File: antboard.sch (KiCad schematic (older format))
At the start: 0 parts

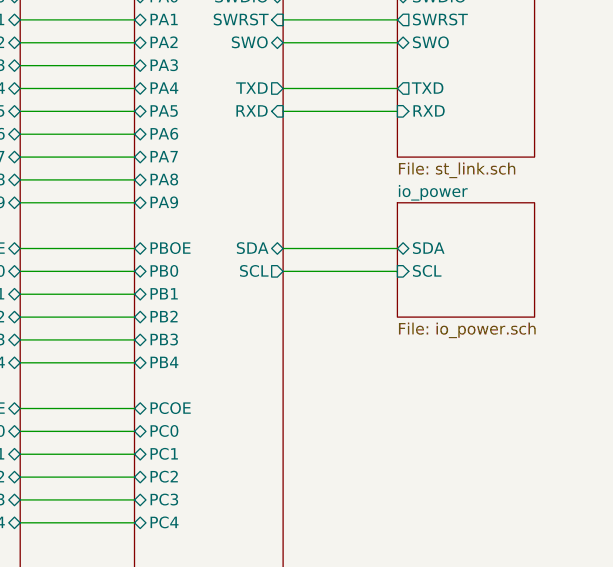
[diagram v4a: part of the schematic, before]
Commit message: sch, pcb: Add ADC to read set IO voltages
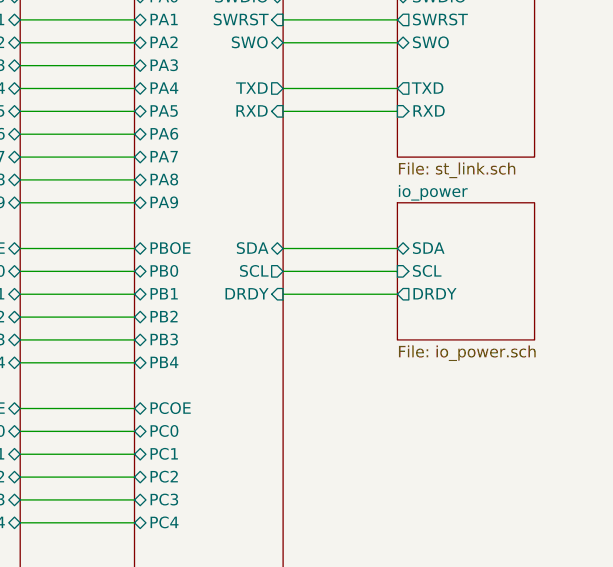
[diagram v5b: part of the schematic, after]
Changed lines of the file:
@@
 F31 "SDA" B R 5900 3600 50
 F32 "SCL" O R 5900 3700 50
+F33 "DRDY" I R 5900 3800 50
 $EndSheet
 $Sheet
@@
 $EndSheet
 $Sheet
-S 6400 3400 600  500
+S 6400 3400 600  600
 U 5EA8F1AB
 F0 "io_power" 50
@@
 F2 "SDA" B L 6400 3600 50
 F3 "SCL" I L 6400 3700 50
+F4 "DRDY" O L 6400 3800 50
 $EndSheet
 Wire Wire Line
@@
 Wire Wire Line
 	6400 3700 5900 3700
+Wire Wire Line
+	5900 3800 6400 3800
 $EndSCHEMATC

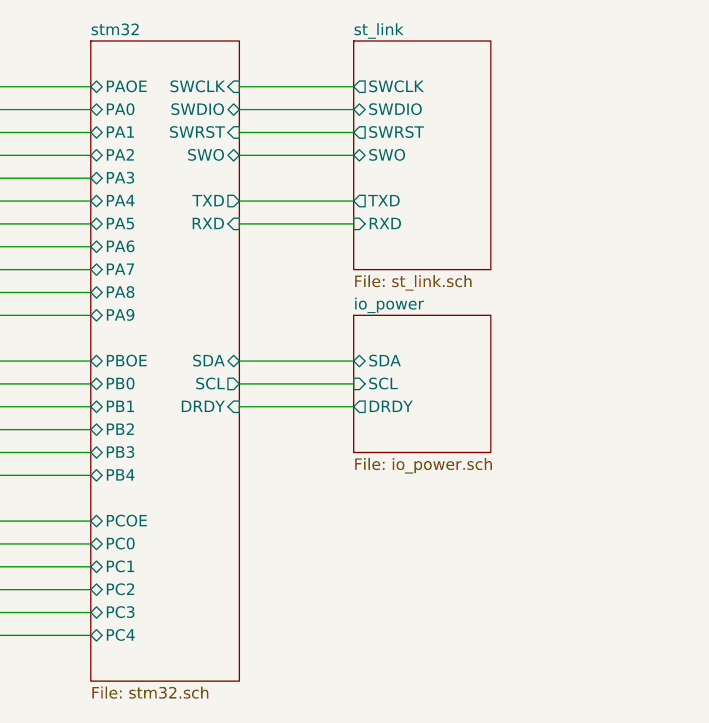
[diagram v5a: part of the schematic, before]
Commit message: sch, pcb: Add USB hub to have a single USB port
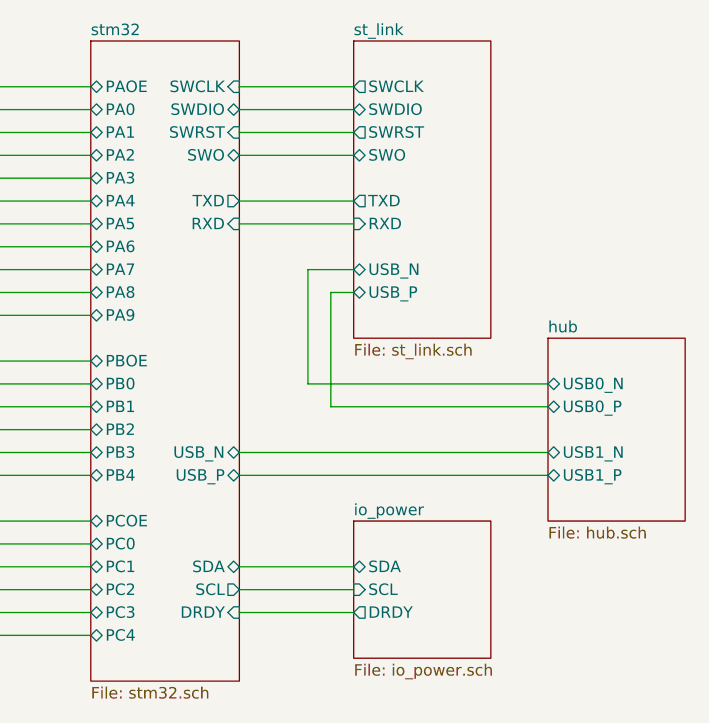
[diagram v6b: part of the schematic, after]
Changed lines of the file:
@@
 EESchema Schematic File Version 4
+LIBS:antboard-cache
 EELAYER 30 0
 EELAYER END
 $Descr A4 11693 8268
 encoding utf-8
-Sheet 1 5
+Sheet 1 6
 Title "STM32 devboard with .05\" headers"
 Date "2019-11-26"
@@
 $EndDescr
 $Sheet
-S 6400 2200 600  1000
+S 6400 2200 600  1300
 U 5DF7E971
 F0 "st_link" 50
@@
 F6 "TXD" O L 6400 2900 50
 F7 "RXD" I L 6400 3000 50
+F8 "USB_N" B L 6400 3200 50
+F9 "USB_P" B L 6400 3300 50
 $EndSheet
 $Sheet
@@
 F29 "PC3" B L 5250 4700 50
 F30 "PC4" B L 5250 4800 50
-F31 "SDA" B R 5900 3600 50
-F32 "SCL" O R 5900 3700 50
-F33 "DRDY" I R 5900 3800 50
+F31 "SDA" B R 5900 4500 50
+F32 "SCL" O R 5900 4600 50
+F33 "DRDY" I R 5900 4700 50
+F34 "USB_N" B R 5900 4000 50
+F35 "USB_P" B R 5900 4100 50
 $EndSheet
 $Sheet
@@
 $EndSheet
 $Sheet
-S 6400 3400 600  600
+S 6400 4300 600  600
 U 5EA8F1AB
 F0 "io_power" 50
 F1 "io_power.sch" 50
-F2 "SDA" B L 6400 3600 50
-F3 "SCL" I L 6400 3700 50
-F4 "DRDY" O L 6400 3800 50
+F2 "SDA" B L 6400 4500 50
+F3 "SCL" I L 6400 4600 50
+F4 "DRDY" O L 6400 4700 50
 $EndSheet
 Wire Wire Line
@@
 	6400 3000 5900 3000
 Wire Wire Line
-	5900 3600 6400 3600
+	5900 4500 6400 4500
 Wire Wire Line
-	6400 3700 5900 3700
+	6400 4600 5900 4600
 Wire Wire Line
-	5900 3800 6400 3800
+	5900 4700 6400 4700
+$Sheet
+S 7250 3500 600  800
+U 5E157F68
+F0 "hub" 50
+F1 "hub.sch" 50
+F2 "USB0_N" B L 7250 3700 50
+F3 "USB0_P" B L 7250 3800 50
+F4 "USB1_N" B L 7250 4000 50
+F5 "USB1_P" B L 7250 4100 50
+$EndSheet
+Wire Wire Line
+	5900 4000 7250 4000
+Wire Wire Line
+	7250 4100 5900 4100
+Wire Wire Line
+	6400 3300 6300 3300
+Wire Wire Line
+	6300 3300 6300 3800
+Wire Wire Line
+	6300 3800 7250 3800
+Wire Wire Line
+	7250 3700 6200 3700
+Wire Wire Line
+	6200 3700 6200 3200
+Wire Wire Line
+	6200 3200 6400 3200
 $EndSCHEMATC
